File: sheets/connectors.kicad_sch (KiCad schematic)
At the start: 9 parts

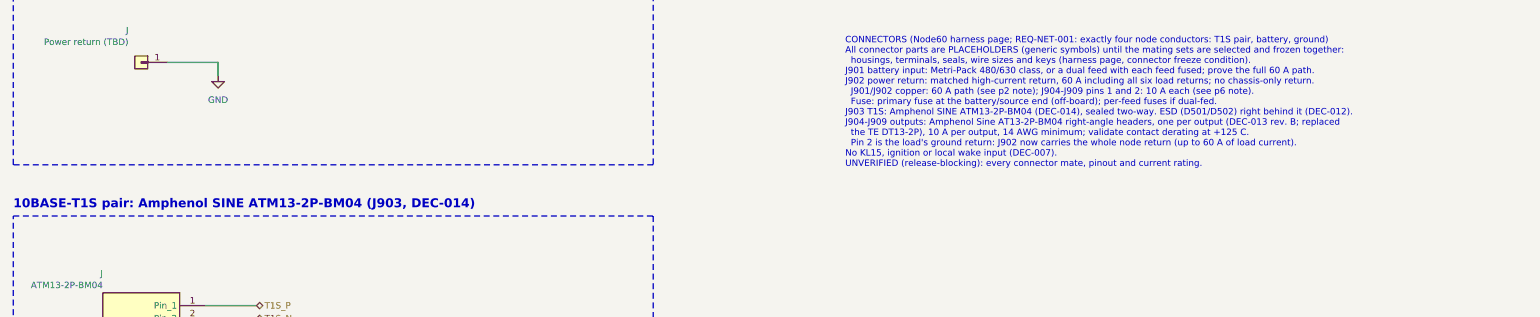
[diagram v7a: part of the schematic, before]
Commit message: Pin DropOut library to main 618de03 (PR #35 merged)
The re-pin also brings library PRs #31, #33 and #34 (manufacturer names,
ATM13 Notes, catalog data). Their field changes are copied into the
schematic so every placed symbol matches the library: "Amphenol Sine
Systems", "Stackpole Electronics", "Murata", and the full ATM13 Notes.

Co-Authored-By: Claude Opus 5.5 <noreply@anthropic.com>
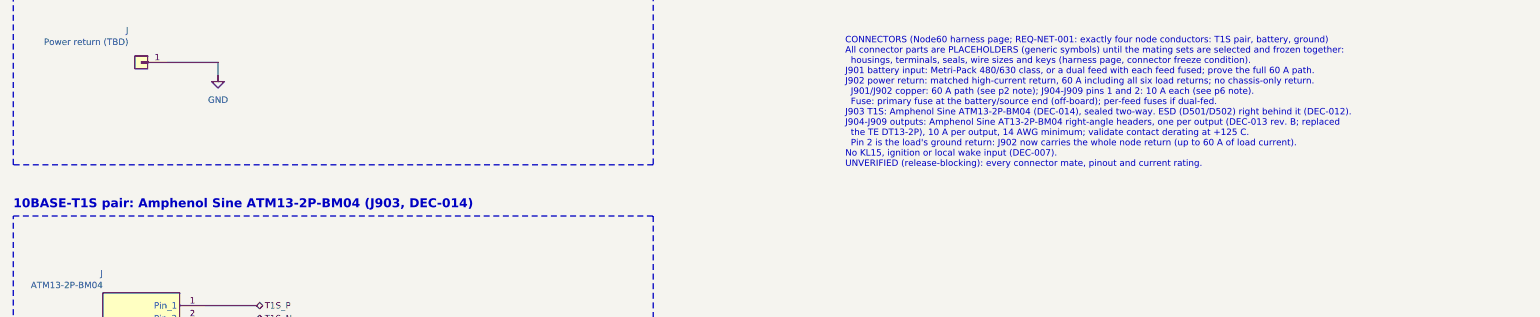
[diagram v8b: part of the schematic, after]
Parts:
- J: Manufacturer Amphenol SINE Systems -> Amphenol Sine Systems; Notes Mates the ATM06-2S plug (size 20 sockets). Fixed by 3x -> Mates the ATM06-2S plug (size 20 sockets). Fixed by 3x #4-2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
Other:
- note added: "10BASE-T1S pair: Amphenol Sine ATM13-2P-BM04 (J903, DEC-014)"
- note removed: "10BASE-T1S pair: Amphenol SINE ATM13-2P-BM04 (J903, DEC-014)"
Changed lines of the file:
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@@
 		)
 	)
-	(text "10BASE-T1S pair: Amphenol SINE ATM13-2P-BM04 (J903, DEC-014)"
+	(text "10BASE-T1S pair: Amphenol Sine ATM13-2P-BM04 (J903, DEC-014)"
 		(exclude_from_sim no)
 		(at 25.4 151.13 0)
@@
 			)
 		)
-		(property "Description" "Amphenol SINE BoardLock ATM13 2-pin right-angle PCB receptacle with flange seal, 4.20 mm pitch, tin-plated size 20 pins, potting, 7.5 A, 250 V, IP67 mated, -55 to +125 °C; mates ATM06-2S"
+		(property "Description" "Amphenol Sine BoardLock ATM13 2-pin right-angle PCB receptacle with flange seal, 4.20 mm pitch, tin-plated size 20 pins, potting, 7.5 A, 250 V, IP67 mated, -55 to +125 °C; mates ATM06-2S"
 			(at 50.8 172.72 0)
 			(effects
@@
 			)
 		)
-		(property "Manufacturer" "Amphenol SINE Systems"
+		(property "Manufacturer" "Amphenol Sine Systems"
 			(at 50.8 172.72 0)
 			(effects
@@
 			)
 		)
-		(property "Notes" "Mates the ATM06-2S plug (size 20 sockets). Fixed by 3x"
+		(property "Notes" "Mates the ATM06-2S plug (size 20 sockets). Fixed by 3x #4-20 thread-forming screws from the solder side (0.68-1.13 N-m). Pin numbering from the drawing's mounting-face view; verify on a sample."
 			(at 50.8 172.72 0)
 			(effects
@@
 		)
 	)
-	(text "CONNECTORS (Node60 harness page; REQ-NET-001: exactly four node conductors: T1S pair, battery, ground)\nAll connector parts are PLACEHOLDERS (generic symbols) until the mating sets are selected and frozen together:\n  housings, terminals, seals, wire sizes and keys (harness page, connector freeze condition).\nJ901 battery input: Metri-Pack 480/630 class, or a dual feed with each feed fused; prove the full 60 A path.\nJ902 power return: matched high-current return, 60 A including all six load returns; no chassis-only return.\n  J901/J902 copper: 60 A path (see p2 note); J904-J909 pins 1 and 2: 10 A each (see p6 note).\n  Fuse: primary fuse at the battery/source end (off-board); per-feed fuses if dual-fed.\nJ903 T1S: Amphenol SINE ATM13-2P-BM04 (DEC-014), sealed two-way. ESD (D501/D502) right behind it (DEC-012).\nJ904-J909 outputs: Amphenol Sine AT13-2P-BM04 right-angle headers, one per output (DEC-013 rev. B; replaced\n  the TE DT13-2P), 10 A per output, 14 AWG minimum; validate contact derating at +125 C.\n  Pin 2 is the load's ground return: J902 now carries the whole node return (up to 60 A of load current).\nNo KL15, ignition or local wake input (DEC-007).\nUNVERIFIED (release-blocking): every connector mate, pinout and current rating.\n"
+	(text "CONNECTORS (Node60 harness page; REQ-NET-001: exactly four node conductors: T1S pair, battery, ground)\nAll connector parts are PLACEHOLDERS (generic symbols) until the mating sets are selected and frozen together:\n  housings, terminals, seals, wire sizes and keys (harness page, connector freeze condition).\nJ901 battery input: Metri-Pack 480/630 class, or a dual feed with each feed fused; prove the full 60 A path.\nJ902 power return: matched high-current return, 60 A including all six load returns; no chassis-only return.\n  J901/J902 copper: 60 A path (see p2 note); J904-J909 pins 1 and 2: 10 A each (see p6 note).\n  Fuse: primary fuse at the battery/source end (off-board); per-feed fuses if dual-fed.\nJ903 T1S: Amphenol Sine ATM13-2P-BM04 (DEC-014), sealed two-way. ESD (D501/D502) right behind it (DEC-012).\nJ904-J909 outputs: Amphenol Sine AT13-2P-BM04 right-angle headers, one per output (DEC-013 rev. B; replaced\n  the TE DT13-2P), 10 A per output, 14 AWG minimum; validate contact derating at +125 C.\n  Pin 2 is the load's ground return: J902 now carries the whole node return (up to 60 A of load current).\nNo KL15, ignition or local wake input (DEC-007).\nUNVERIFIED (release-blocking): every connector mate, pinout and current rating.\n"
 		(exclude_from_sim no)
 		(at 190.5 116.84 0)
